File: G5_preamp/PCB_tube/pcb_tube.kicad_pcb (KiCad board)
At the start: 2 copper layers, 100 x 47 mm, 41 parts, among them J1 PSU_TUBE, J2 PCB_TUBE, Q1 MPS751, Q2 IRF740, U1 ECC83, U2 ECC83, U3 MC34063AP

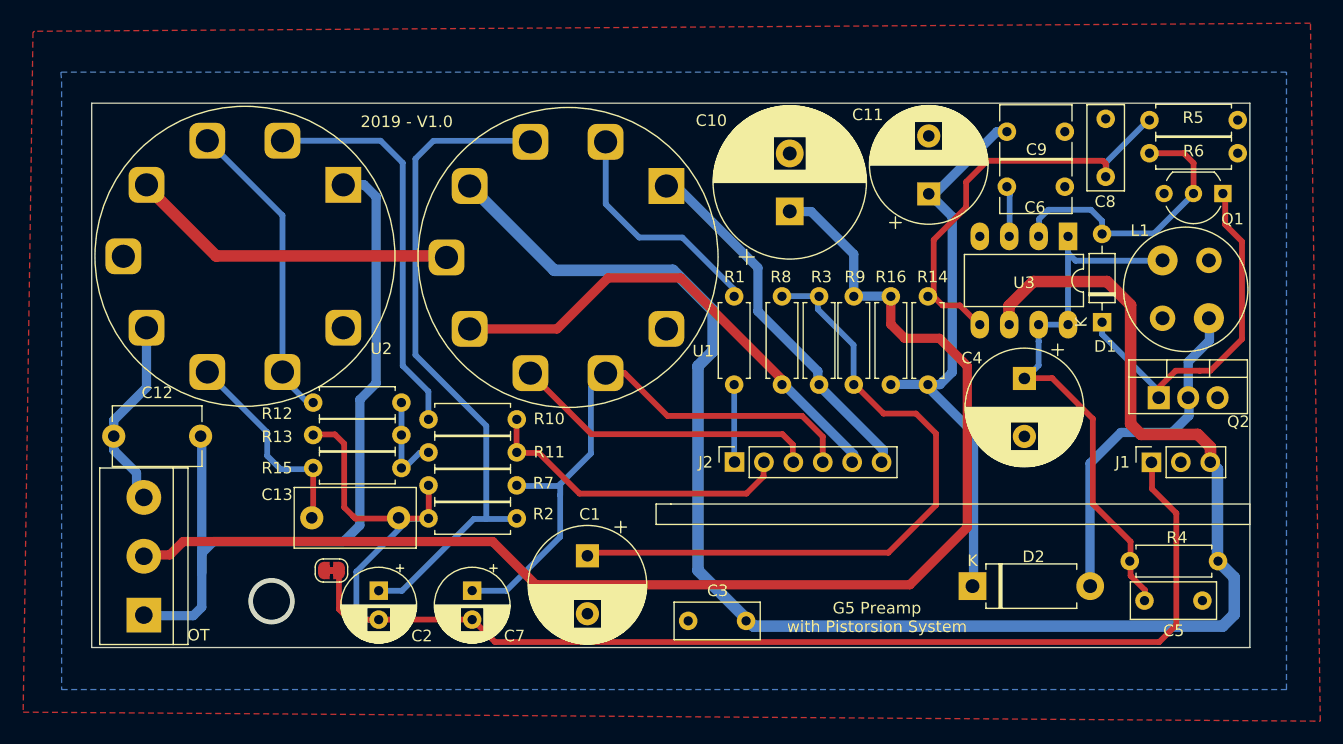
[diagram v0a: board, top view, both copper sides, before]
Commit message: DC-DC move
DC-DC Converter move from PCB_tube to PCB_main
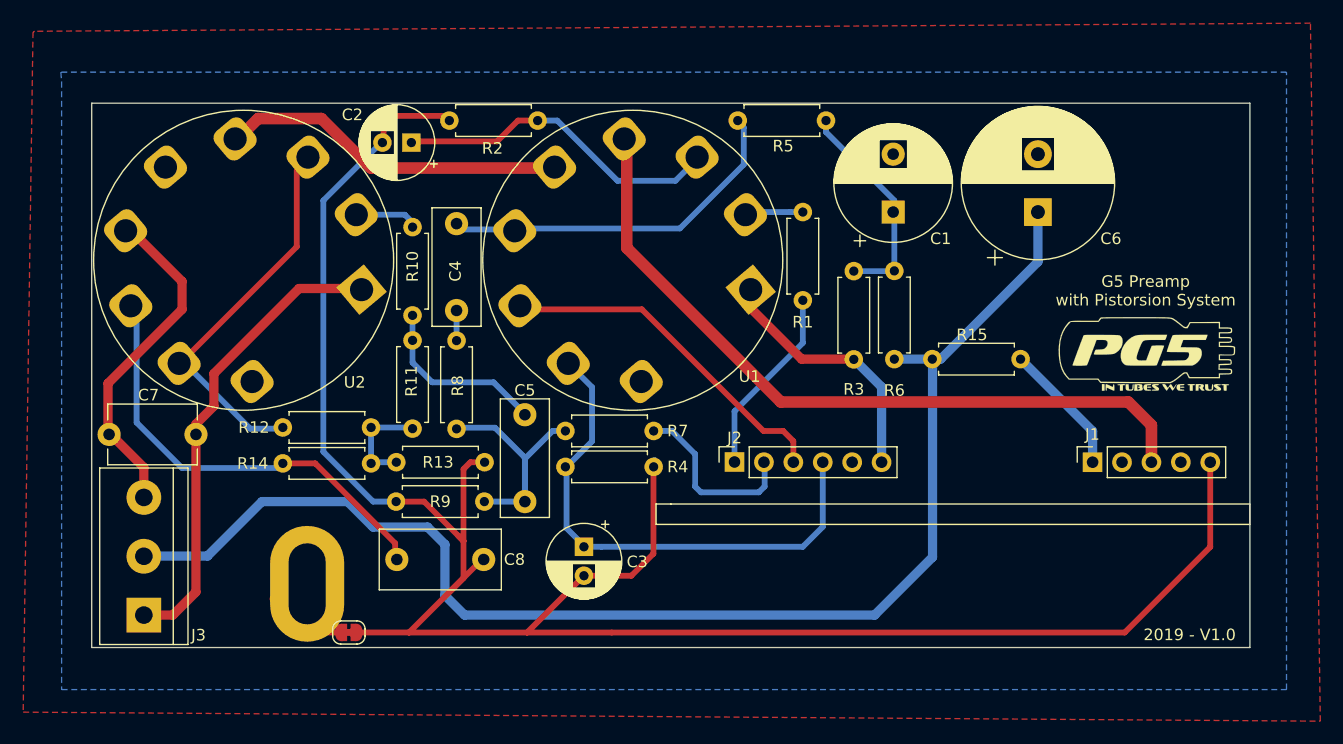
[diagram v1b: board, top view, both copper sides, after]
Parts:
- removed C10: 22µF/350v, Capacitor_THT:CP_Radial_D13.0mm_P5.00mm
- removed C11: 4.7µ/350V, Capacitor_THT:CP_Radial_D10.0mm_P5.00mm
- removed C13: 100n, Capacitor_THT:C_Rect_L10.3mm_W5.0mm_P7.50mm_MKS4
- removed the C3 at (86.5, 97.7)
- removed C9: 10n/400V, Capacitor_THT:C_Disc_D6.0mm_W4.4mm_P5.00mm
- removed D1: 1N4148, Diode_THT:D_DO-35_SOD27_P7.62mm_Horizontal
- removed D2: BYV26, Diode_THT:D_DO-15_P10.16mm_Horizontal
- removed L1: 220µH/1.5A, ProjectLib:L_Radial_D10.5mm_P5.00mm_MuRATA_1200RS
- removed Q1: MPS751, Package_TO_SOT_THT:TO-92_Inline_Wide
- removed Q2: IRF740, Package_TO_SOT_THT:TO-220-3_Vertical
- removed the R14 at (102.2, 77.3)
- removed the R5 at (121.3, 54.5)
- removed the R6 at (121.3, 57.3)
- removed U3: MC34063AP, Package_DIP:DIP-8_W7.62mm_LongPads
- added R8: 470k, Resistor_THT:R_Axial_DIN0207_L6.3mm_D2.5mm_P7.62mm_Horizontal, F.Cu at (61.5, 73.5)
- added R9: 470k, Resistor_THT:R_Axial_DIN0207_L6.3mm_D2.5mm_P7.62mm_Horizontal, F.Cu at (63.9, 87.4)
- added REF**: MountingHole_3.2mm_M3_Pad, MountingHole:MountingHole_3.2mm_M3_Pad, F.Cu at (48.6, 94.5)
- added REF**: PG5_Logo_15mm_SilkScreen, Symbol:PG5_Logo_15mm_SilkScreen, F.Cu at (121.1, 74.4)
- C4: value 470µ -> 22nF; footprint Capacitor_THT:CP_Radial_D10.0mm_P5.00mm -> Capacitor_THT:C_Rect_L10.0mm_W4.0mm_P7.50mm_MKS4
- C5: value 100n -> 22nF; footprint Capacitor_THT:C_Rect_L7.2mm_W3.0mm_P5.00mm_FKS2_FKP2_MKS2_MKP2 -> Capacitor_THT:C_Rect_L10.0mm_W4.0mm_P7.50mm_MKS4
- C6: value 470p -> 22µF/350v; footprint Capacitor_THT:C_Disc_D6.0mm_W4.4mm_P5.00mm -> Capacitor_THT:CP_Radial_D13.0mm_P5.00mm
- C8: footprint Capacitor_THT:C_Rect_L7.2mm_W3.0mm_P5.00mm_FKS2_FKP2_MKS2_MKP2 -> Capacitor_THT:C_Rect_L10.3mm_W5.0mm_P7.50mm_MKS4
- J1: footprint Connector_PinSocket_2.54mm:PinSocket_1x03_P2.54mm_Vertical -> Connector_PinSocket_2.54mm:PinSocket_1x05_P2.54mm_Vertical
- R4: value 0.22R -> 1.8k
- R7: value 1.8k -> 100k
- moved C8 69.6 mm to (56.3, 92.4), turned to 0 degrees
- moved R4 56.9 mm to (70.9, 84.4), turned to 0 degrees
- moved C5 55.9 mm to (67.4, 79.9), turned to 270 degrees
- moved C4 49.4 mm to (61.5, 70.9), turned to 90 degrees
- moved C1 39.7 mm to (99.2, 62.4), turned to 90 degrees
- moved C2 38.8 mm to (57.6, 56.4), turned to 180 degrees
- moved R2 34.4 mm to (68.5, 54.5)
- moved R10 16.7 mm to (57.7, 63.7), turned to 270 degrees
- moved R5 15.6 mm to (93.4, 54.5), turned to 180 degrees
- moved U1 11.5 mm to (86.9, 69.1), turned to 220 degrees
- moved R15 11.4 mm to (110.2, 75.1), turned to 180 degrees
- moved C3 10.4 mm to (72.5, 91.3)
- moved R1 9.39 mm to (91.4, 62.4)
- moved U2 9.19 mm to (53.3, 69.1), turned to 220 degrees
- moved R6 6.45 mm to (99.3, 75.1), turned to 90 degrees
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- renumbered C7 to C3, C12 to C7, OT to J3, R15 to R14, R16 to R15, R8 to R5, R9 to R6
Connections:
- C4 pad 1: /PEAK -> Net-(C4-Pad1)
- C4 pad 2: GNDREF -> Net-(C4-Pad2)
- C5 pad 1: /PEAK -> Net-(C5-Pad1)
- C5 pad 2: GNDREF -> Net-(C5-Pad2)
- C6 pad 1: Net-(C6-Pad1) -> /A+
- C8 pad 2: GNDREF -> GNDS
- J1 pad 1: GNDS -> /HT2
- J1 pad 2: GNDREF -> Net-(J1-Pad2)
- J1 pad 3: /DC_IN -> /24VDC
- J2 pad 2: /G_V2 -> /BOOST
- J2 pad 5: /A_V1B -> Net-(J2-Pad5)
- R10 pad 2: /G_V2 -> Net-(C5-Pad1)
- R11 pad 2: /G_V2 -> Net-(C5-Pad1)
- R14 pad 1: Net-(C13-Pad1) -> Net-(C8-Pad1)
- R4 pad 1: /DC_IN -> /K_V1B
- R4 pad 2: /PEAK -> GNDS
- R5 pad 2: /A_V1B -> Net-(C4-Pad2)
- R7 pad 1: /K_V1B -> Net-(C5-Pad2)
- R7 pad 2: GNDS -> /BOOST
- U1 pad 4: /DC_IN -> /24VDC
- U1 pad 6: /A_V1B -> Net-(C4-Pad2)
- U1 pad 9: (no net) -> Net-(U1-Pad9)
- U2 pad 7: Net-(C13-Pad1) -> Net-(C8-Pad1)
- U2 pad 9: (no net) -> Net-(U2-Pad9)
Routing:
- net /DC_IN: track 144.7 -> 0.00 mm
- net /24VDC: track 0.00 -> 64.7 mm
- net GNDS: track 125.2 -> 181.0 mm
- net /PEAK: track 49.2 -> 0.00 mm
- net /A_V1B: track 42.5 -> 0.00 mm
- net Net-(C1-Pad1): track 58.7 -> 19.4 mm
- net /HT2: track 50.6 -> 11.5 mm
- net Net-(D1-Pad1): track 31.7 -> 0.00 mm
- net Net-(C4-Pad2): track 0.00 -> 31.2 mm
- net /HT1: track 31.0 -> 0.00 mm
- net Net-(C2-Pad1): track 58.7 -> 28.7 mm
- net Net-(R10-Pad1): track 34.3 -> 5.50 mm
- net /A_V2B: track 68.9 -> 40.9 mm
- net /G_V2: track 28.0 -> 0.00 mm
- net Net-(D1-Pad2): track 24.4 -> 0.00 mm
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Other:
- net class 24DVC removed
- net class 24VDC added: clearance 0.8, trace_width 1, via_dia 1, via_drill 0.4

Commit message: Gerber export
Last MAJ with GERBER
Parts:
- renumbered U1 to V1, U2 to V2
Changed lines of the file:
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@@
     (descr "Valve Noval-B9A Belton-VT9-PT Socket, Made by script https://github.com/pointhi/kicad-footprint-generator/scripts/Valves, http://www.belton.co.kr/inc/downfile.php?seq=58&file=pdf")
     (tags Valve_Noval-B9A_Belton-VT9-PT_Socket)
-    (fp_text reference U1 (at 4.897512 -5.681055) (layer F.SilkS)
+    (fp_text reference V1 (at 4.897512 -5.681055) (layer F.SilkS)
       (effects (font (size 1 1) (thickness 0.15)))
     )
@@
     (descr "Valve Noval-B9A Belton-VT9-PT Socket, Made by script https://github.com/pointhi/kicad-footprint-generator/scripts/Valves, http://www.belton.co.kr/inc/downfile.php?seq=58&file=pdf")
     (tags Valve_Noval-B9A_Belton-VT9-PT_Socket)
-    (fp_text reference U2 (at 5.601928 -5.742683) (layer F.SilkS)
+    (fp_text reference V2 (at 5.601928 -5.742683) (layer F.SilkS)
       (effects (font (size 1 1) (thickness 0.15)))
     )
